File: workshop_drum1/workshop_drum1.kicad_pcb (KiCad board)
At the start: 2 copper layers, 1 part, among them J1 JACK-MONO

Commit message: ready to build schematic
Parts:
- removed J1: JACK-MONO, zfoot:Jack_Instrument
- added BB10: BreadBoardStrip, zfoot:BreadBoardStrip, F.Cu at (14.0, -2.54)
- added BB11: BreadBoardStrip, zfoot:BreadBoardStrip, F.Cu at (1.27, 2.54)
- added BB12: BreadBoardStrip, zfoot:BreadBoardStrip, F.Cu at (14.0, 0.00)
- added BB5: BreadBoardStrip, zfoot:BreadBoardStrip, F.Cu at (1.27, -5.08)
- added BB6: BreadBoardStrip, zfoot:BreadBoardStrip, F.Cu at (1.27, 5.08)
- added BB7: BreadBoardStrip, zfoot:BreadBoardStrip, F.Cu at (1.27, -2.54)
- added BB8: BreadBoardStrip, zfoot:BreadBoardStrip, F.Cu at (1.27, 7.62)
- added BB9: BreadBoardStrip, zfoot:BreadBoardStrip, F.Cu at (1.27, 0.00)
- added GND1: GNDStrip, zfoot:GNDStrip, F.Cu at (1.27, 10.2)
- added PWR1: GNDStrip, zfoot:GNDStrip, F.Cu at (14.0, -5.08)
- added U1: LM358, 4ms-footprints:DIP_8pin_TL082_TH, F.Cu at (43.6, -1.60)
- added U2: HEX_INV_TRI, 4ms-footprints:DIP-14_W7.62mm, F.Cu at (3.81, -5.08)

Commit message: schematic laid out - started PCB
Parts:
- added BB1: BreadBoardStrip, zfoot:BreadBoardStrip, F.Cu at (174.0, 61.0)
- added Button_ON1: SPST_small, zfoot:SPST_Wired, F.Cu at (77.5, 90.2)
- added C1: 100uF, 4ms-footprints:Cap_Electrolytic_TH, F.Cu at (115.6, 135.9)
- added C2: 1uF, 4ms-footprints:Cap_Electrolytic_TH, F.Cu at (113.0, 97.8)
- added C3: 10uF, 4ms-footprints:Cap_Electrolytic_TH, F.Cu at (130.8, 135.9)
- added C4: 1uF, 4ms-footprints:Cap_Electrolytic_TH, F.Cu at (152.4, 67.3)
- added C5: 220nF, 4ms-footprints:Cap_Ceramic_TH, F.Cu at (182.9, 61.0)
- added D1: 4002, 4ms-footprints:Diode_BAT-85S_TH, F.Cu at (102.9, 133.3)
- added D2: 4148, 4ms-footprints:Diode_BAT-85S_TH, F.Cu at (118.1, 81.3)
- added DECAY1: A500k-A1M, zfoot:Pot_Wired, F.Cu at (125.7, 82.5)
- added J1: 9v_Battery_Clip, zfoot:Jack_DC, F.Cu at (91.4, 128.3)
- added J2: Trigger_Input, zfoot:Jack_Instrument, F.Cu at (72.4, 90.2)
- added J3: Output, zfoot:Jack_Instrument, F.Cu at (196.8, 54.6)
- added ON/OFF_LED1: LED-C1-A2, LED-C1-A2-3MM-VERT, F.Cu at (96.5, 139.7)
- added Osc_Select1: SPDT_small, zfoot:SPDT_Wired, F.Cu at (171.4, 58.4)
- added PITCH1: B50k, zfoot:Pot_Wired, F.Cu at (157.5, 59.7)
- added PWR2: SPST_small, zfoot:SPST_Wired, F.Cu at (96.5, 128.3)
- added R1: 1k, 4ms-footprints:Resistor_TH_300, F.Cu at (91.4, 95.2)
- added R2: 1k, 4ms-footprints:Resistor_TH_300, F.Cu at (104.1, 97.8)
- added R3: 1k, 4ms-footprints:Resistor_TH_300, F.Cu at (104.1, 139.7)
- added R4: 1M, 4ms-footprints:Resistor_TH_300, F.Cu at (104.1, 81.3)
- added R5: 100k, 4ms-footprints:Resistor_TH_300, F.Cu at (118.1, 97.8)
- added R6: 470, 4ms-footprints:Resistor_TH_300, F.Cu at (161.3, 67.3)
- added R7: 1k, 4ms-footprints:Resistor_TH_300, F.Cu at (189.2, 61.0)
- added R8: 470, 4ms-footprints:Resistor_TH_300, F.Cu at (149.9, 76.2)
- added SENSE/STARVE1: A50k, zfoot:Pot_Wired, F.Cu at (88.9, 90.2)
- added Switch_On1: SPST_small, zfoot:SPST_Wired, F.Cu at (82.5, 90.2)
- added Trig_LED1: LED-C1-A2, LED-C1-A2-3MM-VERT, F.Cu at (142.2, 76.2)
- added U3: 78L05, 4ms-footprints:TO-92_Molded_Narrow, F.Cu at (121.9, 135.9)
- PWR1: value GNDStrip -> PWRStrip
- U2: value HEX_INV_TRI -> 7414
- moved BB10 139.2 mm to (138.4, 59.7)
- moved BB11 139.2 mm to (125.7, 64.8)
- moved BB12 139.2 mm to (138.4, 62.2)
- moved BB5 139.2 mm to (125.7, 57.1)
- moved BB6 139.2 mm to (125.7, 67.3)
- moved BB7 139.2 mm to (125.7, 59.7)
- moved BB8 139.2 mm to (125.7, 69.8)
- moved BB9 139.2 mm to (125.7, 62.2)
- moved GND1 139.2 mm to (125.7, 72.4)
- moved PWR1 139.2 mm to (138.4, 57.1)
- moved U2 139.2 mm to (128.3, 57.1)
- moved U1 105.7 mm to (104.1, 85.1)
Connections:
- U1 pad 4: Net-(U1-Pad4) -> GND
- U1 pad 6: Net-(U1-Pad6) -> Net-(PWR1-Pad1)
- U1 pad 7: Net-(U1-Pad7) -> Net-(PWR1-Pad1)
- U1 pad 8: Net-(U1-Pad8) -> +5V
- U2 pad 9: Net-(U2-Pad9) -> GND

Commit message: finished first look of schematic
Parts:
- ON/OFF_LED1, Trig_LED1: footprint LED-C1-A2-3MM-VERT -> zfoot:LED_wired
- moved C3 184.9 mm to (46.4, -28.6), turned to 270 degrees
- moved R8 177.1 mm to (5.71, -26.7)
- moved U3 175.9 mm to (54.6, -26.7), turned to 180 degrees
- moved C1 173.5 mm to (60.3, -28.6), turned to 270 degrees
- moved Trig_LED1 166.6 mm to (3.81, -16.5), turned to 90 degrees
- moved J3 165.9 mm to (61.0, -40.6)
- moved C5 162.9 mm to (52.1, -36.2)
- moved R6 162.6 mm to (37.5, -38.1), turned to 180 degrees
- moved R7 162.4 mm to (59.1, -36.2)
- moved R2 162.2 mm to (5.71, -31.1)
- moved D1 162.1 mm to (55.2, -21.6), turned to 0 degrees
- moved R5 160.3 mm to (29.2, -35.6), turned to 180 degrees
- moved ON/OFF_LED1 160.2 mm to (61.0, -16.5), turned to 270 degrees
- moved DECAY1 158.9 mm to (25.4, -40.6)
- moved R3 157.6 mm to (55.2, -10.2), turned to 270 degrees
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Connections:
- U1 pad 1: Net-(D2-Pad2) -> Net-(PWR1-Pad1)
- U1 pad 2: Net-(R2-Pad1) -> Net-(PWR1-Pad1)
- U1 pad 3: Net-(SENSE/STARVE1-Pad2) -> Net-(C2-Pad1)
- U1 pad 5: Net-(C2-Pad1) -> Net-(SENSE/STARVE1-Pad2)
- U1 pad 6: Net-(PWR1-Pad1) -> Net-(R2-Pad1)
- U1 pad 7: Net-(PWR1-Pad1) -> Net-(D2-Pad2)
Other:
- board outline added: 64.8 x 45 mm

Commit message: CRUISIN'
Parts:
- removed BB1, BB10, BB11, BB12, BB5, BB6, BB7, BB8, BB9: BreadBoardStrip, zfoot:BreadBoardStrip
- added IN1: BreadBoardStrip, zfoot:BreadBoardStrip, F.Cu at (26.8, -10.8)
- added IN2: BreadBoardStrip, zfoot:BreadBoardStrip, F.Cu at (31.9, -10.8)
- added IN3: BreadBoardStrip, zfoot:BreadBoardStrip, F.Cu at (37.0, -10.8)
- added OUT1: BreadBoardStrip, zfoot:BreadBoardStrip, F.Cu at (29.3, -10.8)
- added OUT2: BreadBoardStrip, zfoot:BreadBoardStrip, F.Cu at (34.4, -10.8)
- added OUT3: BreadBoardStrip, zfoot:BreadBoardStrip, F.Cu at (39.5, -10.8)
- added OscSwitchStrip1: BreadBoardStrip, zfoot:BreadBoardStrip, F.Cu at (45.2, -10.8)
- moved PWR1 24.1 mm to (49.5, -10.8), turned to 270 degrees
- moved C4 22.3 mm to (17.1, -21.0)
- moved U2 14.4 mm to (26.8, -13.3), turned to 90 degrees
- moved C2 12.8 mm to (17.1, -29.8)
- moved R6 11.3 mm to (28.6, -31.1), turned to 0 degrees
- moved U3 9.67 mm to (50.8, -17.8), turned to 270 degrees
- moved GND1 7.99 mm to (42.0, -10.8), turned to 270 degrees
- moved U1 6.38 mm to (14.0, -10.8), turned to 0 degrees
- moved R3 4.02 mm to (54.0, -6.35)
- moved C1 2.84 mm to (57.8, -29.8)
- moved D1 2.62 mm to (52.7, -22.2)
- moved C5 2.54 mm to (49.5, -36.2)
- moved J1 2.54 mm to (58.4, -3.81)
- moved J3 2.54 mm to (58.4, -40.6)
- moved ON/OFF_LED1 2.54 mm to (58.4, -16.5)
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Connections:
- U1 pad 1: Net-(PWR1-Pad1) -> Net-(D2-Pad2)
- U1 pad 2: Net-(PWR1-Pad1) -> Net-(R2-Pad1)
- U1 pad 3: Net-(C2-Pad1) -> Net-(SENSE/STARVE1-Pad2)
- U1 pad 5: Net-(SENSE/STARVE1-Pad2) -> Net-(C2-Pad1)
- U1 pad 6: Net-(R2-Pad1) -> Net-(PWR1-Pad1)
- U1 pad 7: Net-(D2-Pad2) -> Net-(PWR1-Pad1)
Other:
- board size 64.8 x 45 mm -> 62.2 x 45 mm

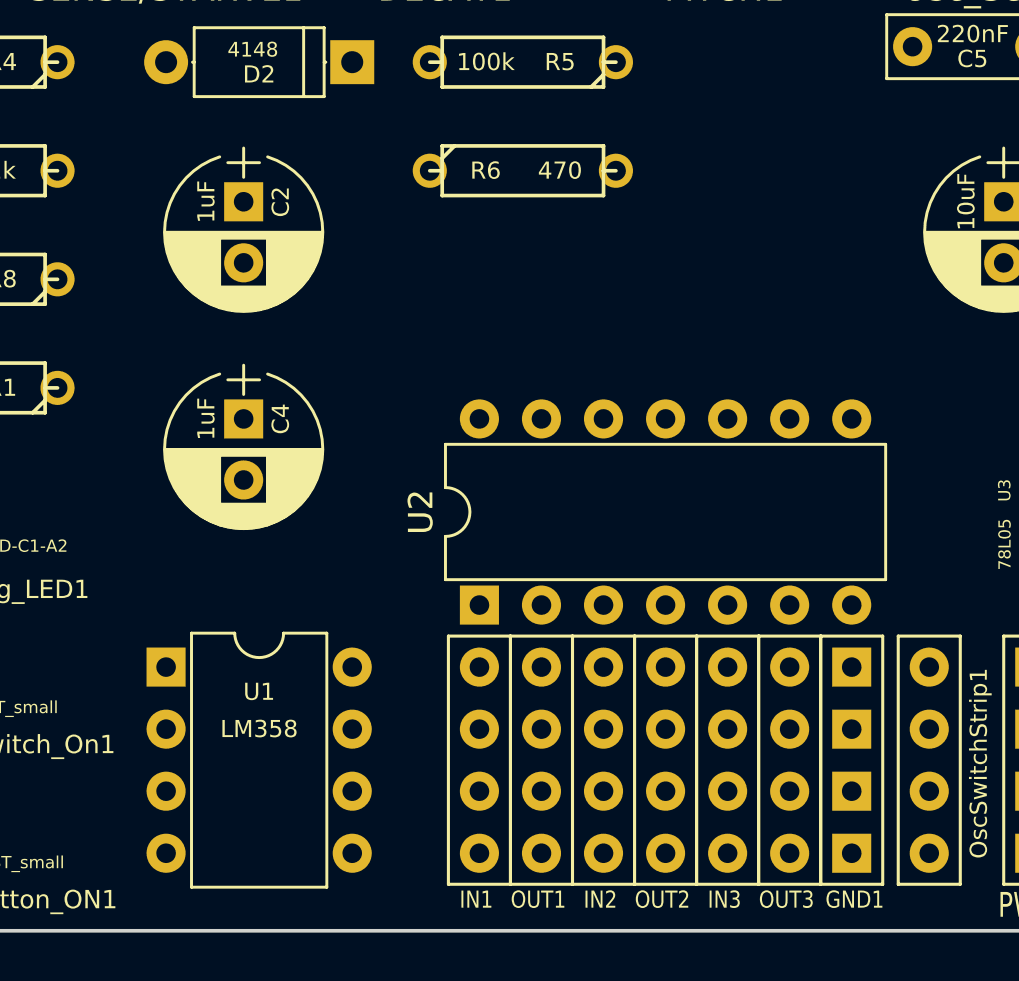
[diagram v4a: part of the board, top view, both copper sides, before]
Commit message: places breadboard section in better spot
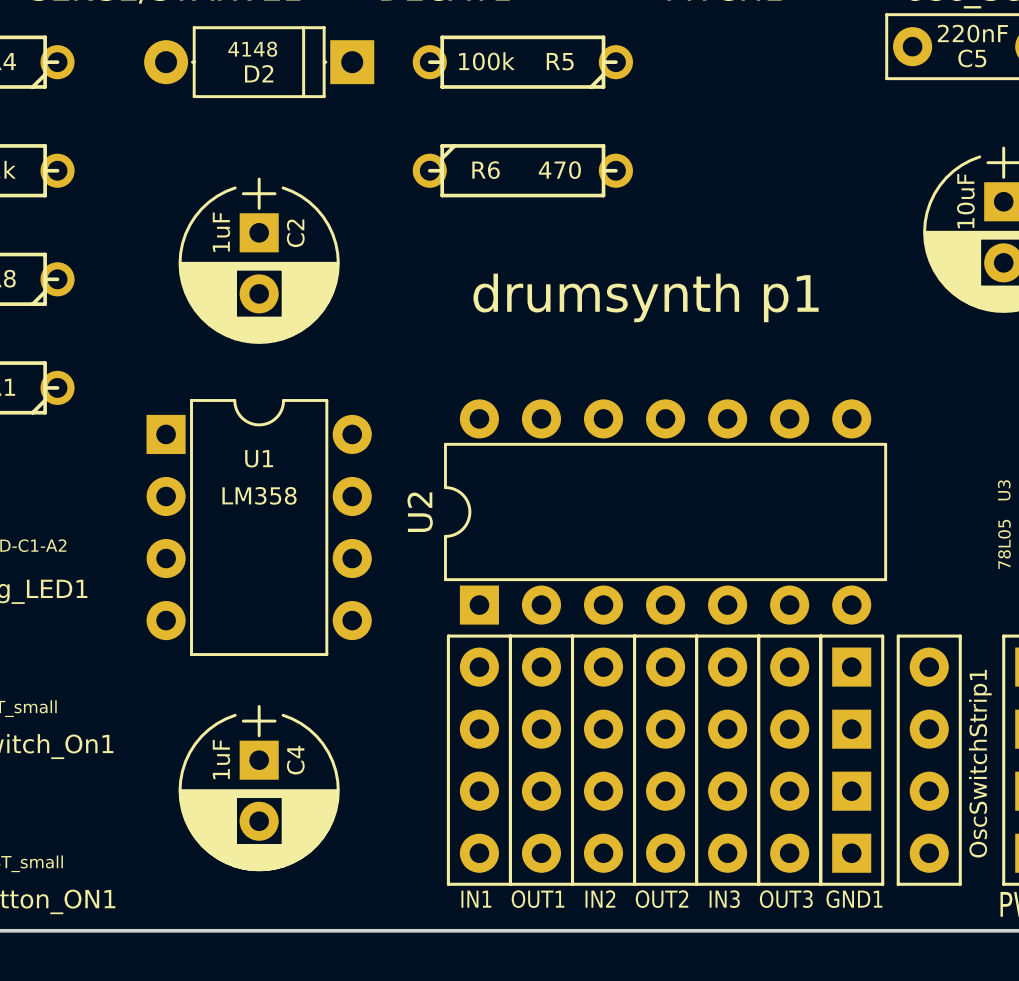
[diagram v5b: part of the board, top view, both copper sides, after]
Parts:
- moved C4 14.0 mm to (17.8, -6.99)
- moved U1 9.53 mm to (14.0, -20.3)
- moved C2 1.42 mm to (17.8, -28.6)
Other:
- board text added: "drumsynth p1"
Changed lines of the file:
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@@
   (general
     (thickness 1.6)
-    (drawings 4)
+    (drawings 5)
     (tracks 0)
     (zones 0)
@@
   )
   (module 4ms-footprints:Cap_Electrolytic_TH (layer F.Cu)
-    (at 17.145 -20.955 270)
+    (at 17.78 -6.985 270)
     (descr "CP, Radial series, Radial, pin pitch=2.50mm, , diameter=6.3mm, Electrolytic Capacitor")
     (tags "CP Radial series Radial pin pitch 2.50mm  diameter 6.3mm Electrolytic Capacitor")
@@
   )
   (module 4ms-footprints:Cap_Electrolytic_TH (layer F.Cu)
-    (at 17.145 -29.845 270)
+    (at 17.78 -28.575 270)
     (descr "CP, Radial series, Radial, pin pitch=2.50mm, , diameter=6.3mm, Electrolytic Capacitor")
     (tags "CP Radial series Radial pin pitch 2.50mm  diameter 6.3mm Electrolytic Capacitor")
@@
   )
   (module 4ms-footprints:DIP_8pin_TL082_TH (layer F.Cu)
-    (at 13.97 -10.795)
+    (at 13.97 -20.32)
     (descr "8-lead dip package, row spacing 7.62 mm (300 mils)")
     (tags "DIL DIP PDIP 2.54mm 7.62mm 300mil")
@@
     )
   )
+  (gr_text "drumsynth p1" (at 33.655 -26.035) (layer F.SilkS)
+    (effects (font (size 1.5 1.5) (thickness 0.3)))
+  )
   (gr_line (start 0 0) (end 62.23 0) (layer Edge.Cuts) (width 0.15))

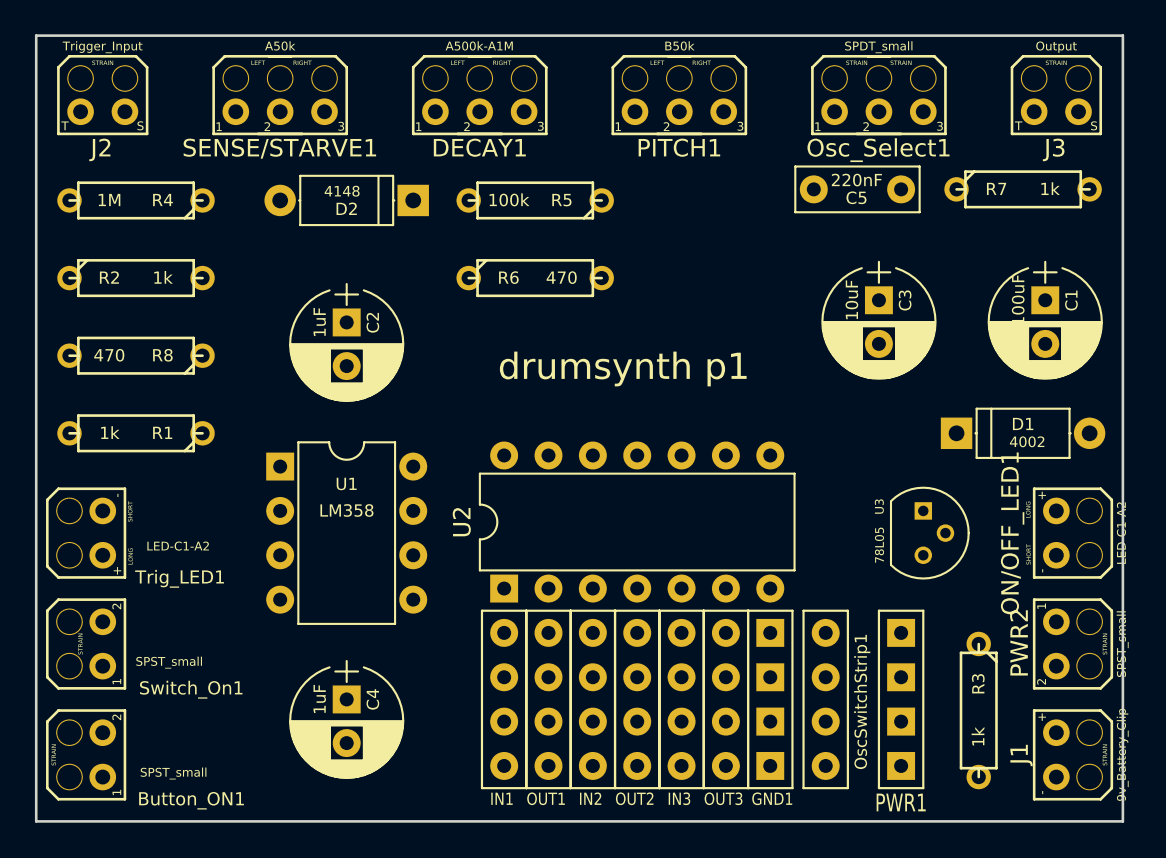
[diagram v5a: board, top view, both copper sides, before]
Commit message: connected traces
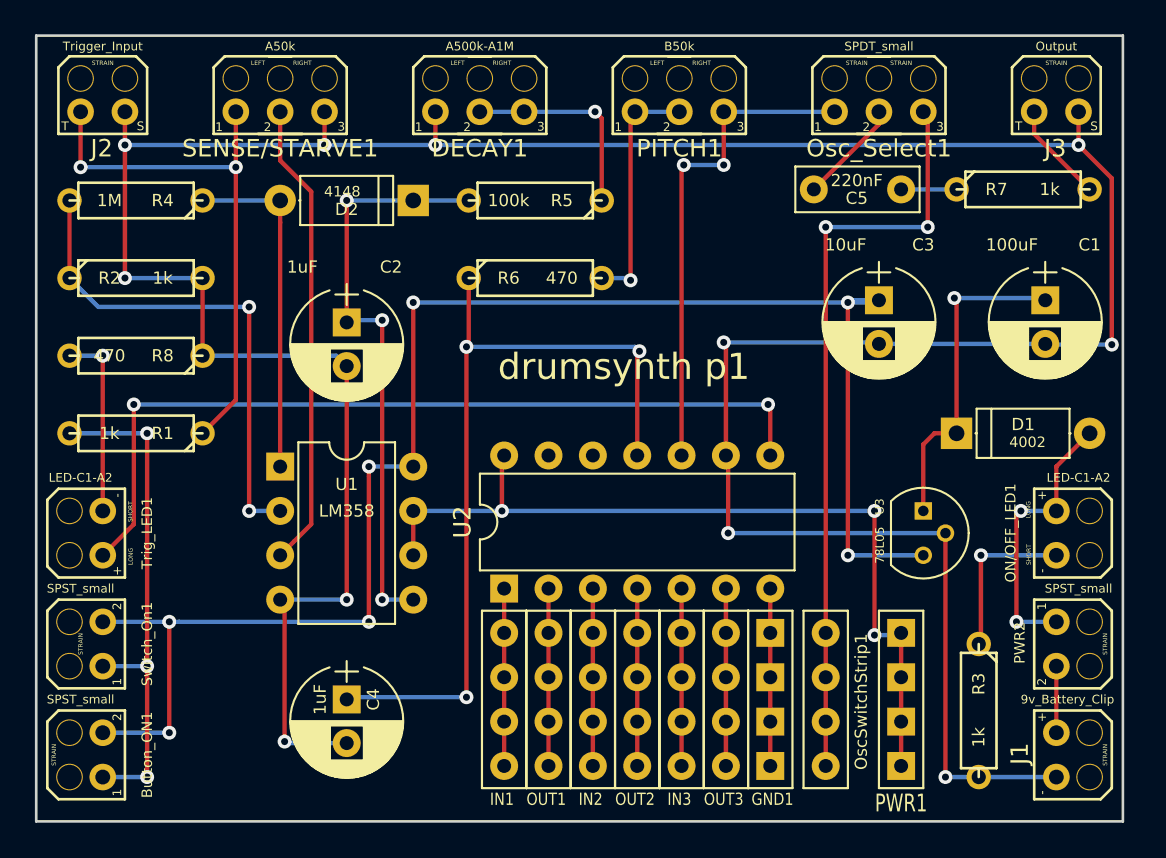
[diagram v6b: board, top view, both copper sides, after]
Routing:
- net GND: track 0.00 -> 194.5 mm, vias 0 -> 11
- net +5V: track 0.00 -> 93.4 mm, vias 0 -> 7
- net Net-(Trig_LED1-Pad2): track 0.00 -> 48.7 mm, vias 0 -> 2
- net Net-(PWR1-Pad1): track 0.00 -> 48.5 mm, vias 0 -> 3
- net Net-(C4-Pad1): track 0.00 -> 47.0 mm, vias 0 -> 3
- net Net-(OscSwitchStrip1-Pad1): track 0.00 -> 43.4 mm, vias 0 -> 2
- net Net-(C2-Pad1): track 0.00 -> 33.8 mm, vias 0 -> 3
- net Net-(J2-Pad1): track 0.00 -> 31.3 mm, vias 0 -> 2
- net Net-(Button_ON1-Pad1): track 0.00 -> 29.2 mm, vias 0 -> 3
- net Net-(R2-Pad1): track 0.00 -> 28.9 mm, vias 0 -> 2
- net Net-(Osc_Select1-Pad1): track 0.00 -> 28.4 mm, vias 0 -> 2
- net Net-(SENSE/STARVE1-Pad2): track 0.00 -> 26.9 mm
- net Net-(D2-Pad2): track 0.00 -> 19.7 mm
- net Net-(C1-Pad1): track 0.00 -> 19.0 mm, vias 0 -> 1
- net Net-(D1-Pad2): track 0.00 -> 16.0 mm, vias 0 -> 2
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
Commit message: ready to send in
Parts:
- added GND2: GNDStrip, zfoot:GNDStripLONG, F.Cu at (26.8, -2.03)
- moved U2 4.70 mm to (26.8, -18.0)
- moved OscSwitchStrip1 3.06 mm to (45.0, -13.8)
- moved GND1 3.05 mm to (42.0, -13.8)
- moved IN1 3.05 mm to (26.8, -13.8)
- moved IN2 3.05 mm to (31.9, -13.8)
- moved IN3 3.05 mm to (37.0, -13.8)
- moved OUT1 3.05 mm to (29.3, -13.8)
- moved OUT2 3.05 mm to (34.4, -13.8)
- moved OUT3 3.05 mm to (39.5, -13.8)
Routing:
- net Net-(GND1-Pad1): track 10.2 -> 31.2 mm
- net Net-(PWR1-Pad1): track 48.5 -> 56.5 mm, vias 3 -> 4
- net GND: track 194.5 -> 187.8 mm, vias 11 -> 10
- net Net-(Osc_Select1-Pad1): track 28.4 -> 22.3 mm, vias 2 -> 0
- net Net-(C4-Pad1): track 47.0 -> 42.7 mm
- net Net-(OscSwitchStrip1-Pad1): track 43.4 -> 40.5 mm
- net Net-(OUT3-Pad1): track 10.2 -> 7.62 mm
- net Net-(OUT2-Pad1): track 10.2 -> 7.62 mm
- net Net-(OUT1-Pad1): track 10.2 -> 7.62 mm
- net Net-(IN3-Pad1): track 10.2 -> 7.62 mm
- net Net-(IN2-Pad1): track 10.2 -> 7.62 mm
- net Net-(IN1-Pad1): track 10.2 -> 7.62 mm
- net Net-(Trig_LED1-Pad2): track 48.7 -> 46.6 mm, vias 2 -> 1
- net +5V: track 93.4 -> 94.0 mm
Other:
- board text added: "v v v GROUND STRIP v v v"
